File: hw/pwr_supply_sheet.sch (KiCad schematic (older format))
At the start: 14 parts

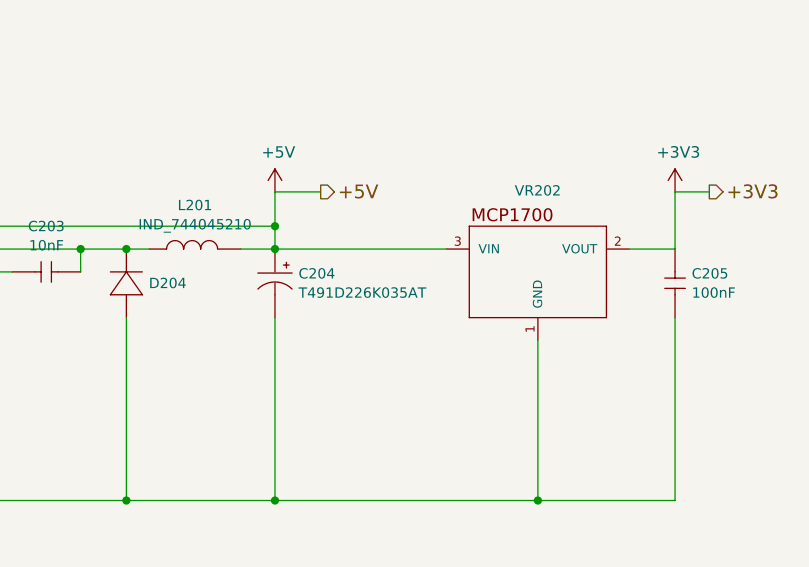
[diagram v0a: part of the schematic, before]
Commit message: 1.4.0 pcb created, tantalum caps changed to bigger ones
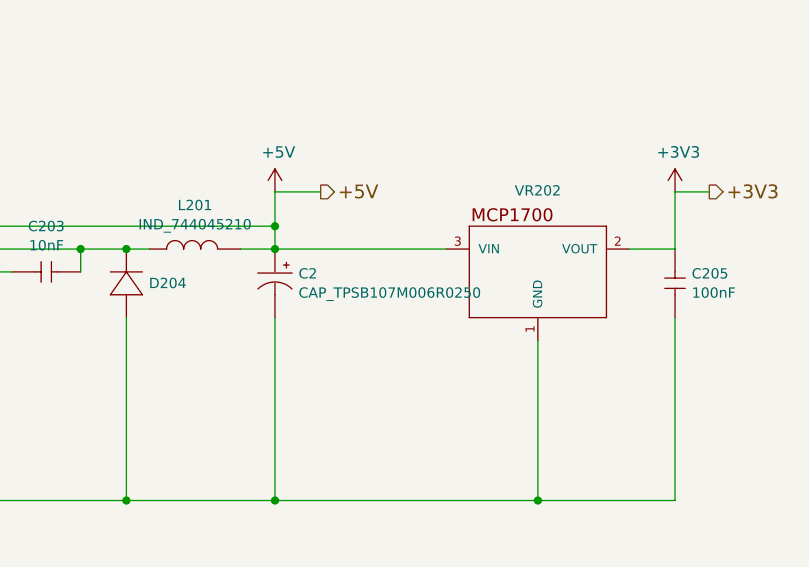
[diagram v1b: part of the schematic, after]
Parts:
- removed C204: T491D226K035AT, kemet:7343, symbol kemet:T491D226K035AT
- added C2: CAP_TPSB107M006R0250, usevolt:1210_CAP, symbol usevolt:CAP_TPSB107M006R0250
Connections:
- net +5V: now also C2.+
- net GND: now also C2.-
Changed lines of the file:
@@
-$EndComp
-$Comp
-L kemet:T491D226K035AT C204
-U 1 1 597AF606
-P 6850 4050
-F 0 "C204" V 6758 4153 45  0000 L CNN
-F 1 "T491D226K035AT" V 6842 4153 45  0000 L CNN
-F 2 "kemet:7343" H 6880 4200 20  0001 C CNN
-F 3 "http://www.farnell.com/datasheets/2121523.pdf?_ga=1.259966538.1948984246.1460023966" H 6850 3990 60  0001 C CNN
-F 4 "399-8375-1-ND" H 7450 4590 60  0001 C CNN "2nd Source Part Number"
-F 5 "Farnell" H 7150 4290 60  0001 C CNN "1st Source"
-F 6 "T491D226K035AT" H 7050 4190 60  0001 C CNN "Manufacturer Part Number"
-F 7 "Digikey" H 7350 4490 60  0001 C CNN "2nd Source"
-F 8 "Kemet" H 6950 4090 60  0001 C CNN "Manufacturer"
-F 9 "1457504" H 7250 4390 60  0001 C CNN "1st Source Part Number"
-	1    6850 4050
-	0    1    1    0
 $EndComp
 $Comp
@@
 	2550 2700 2900 2700
 Connection ~ 2900 2700
+$Comp
+L usevolt:CAP_TPSB107M006R0250 C2
+U 1 1 5C620853
+P 6850 4050
+F 0 "C2" V 6758 4153 45  0000 L CNN
+F 1 "CAP_TPSB107M006R0250" V 6842 4153 45  0000 L CNN
+F 2 "usevolt:1210_CAP" H 6880 4200 20  0001 C CNN
+F 3 "http://datasheets.avx.com/TPS.pdf" H 6850 3990 60  0001 C CNN
+F 4 "AVX Corporation" H 6950 4090 60  0001 C CNN "Manufacturer"
+F 5 "TPSB107M006R0250" H 7050 4190 60  0001 C CNN "Manufacturer Part Number"
+F 6 "Digi-Key" H 7150 4290 60  0001 C CNN "1st Source"
+F 7 "478-4978-1-ND" H 7250 4390 60  0001 C CNN "1st Source Part Number"
+F 8 "Mouser" H 7350 4490 60  0001 C CNN "2nd Source"
+F 9 "581-TPSB107M006R0250" H 7450 4590 60  0001 C CNN "2nd Source Part Number"
+	1    6850 4050
+	0    1    1    0
+$EndComp
 $EndSCHEMATC

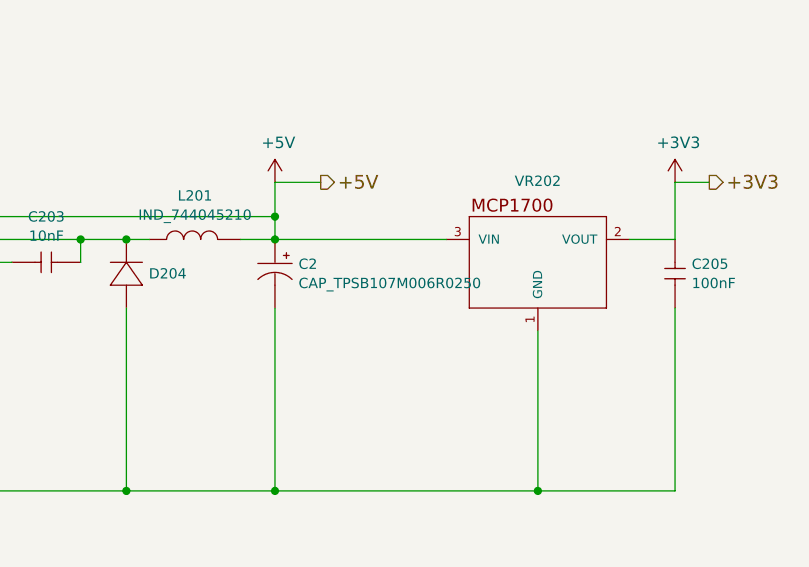
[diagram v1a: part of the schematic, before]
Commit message: hw 1.5.0, 2 ain inputs added
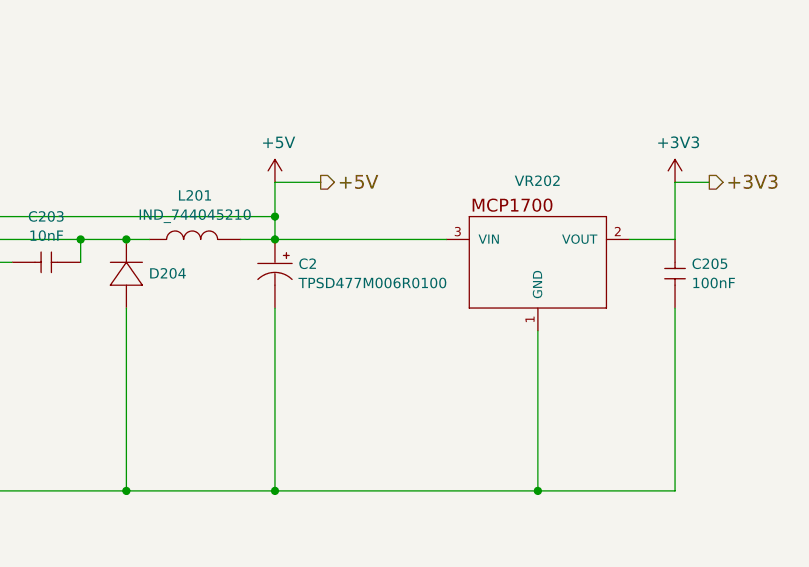
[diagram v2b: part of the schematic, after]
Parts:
- removed C2: CAP_TPSB107M006R0250, usevolt:1210_CAP, symbol usevolt:CAP_TPSB107M006R0250
- added C2: TPSD477M006R0100, usevolt:7343, symbol usevolt:TPSD477M006R0100
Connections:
- net +5V: now also C2.+
- net GND: now also C2.-
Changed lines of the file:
@@
 $Descr A4 11693 8268
 encoding utf-8
-Sheet 2 13
+Sheet 2 14
 Title "Power supply"
 Date "2016-08-20"
@@
 Connection ~ 2900 2700
 $Comp
-L usevolt:CAP_TPSB107M006R0250 C2
-U 1 1 5C620853
+L usevolt:TPSD477M006R0100 C2
+U 1 1 5D04E64E
 P 6850 4050
 F 0 "C2" V 6758 4153 45  0000 L CNN
-F 1 "CAP_TPSB107M006R0250" V 6842 4153 45  0000 L CNN
-F 2 "usevolt:1210_CAP" H 6880 4200 20  0001 C CNN
+F 1 "TPSD477M006R0100" V 6842 4153 45  0000 L CNN
+F 2 "usevolt:7343" H 6880 4200 20  0001 C CNN
 F 3 "http://datasheets.avx.com/TPS.pdf" H 6850 3990 60  0001 C CNN
-F 4 "AVX Corporation" H 6950 4090 60  0001 C CNN "Manufacturer"
-F 5 "TPSB107M006R0250" H 7050 4190 60  0001 C CNN "Manufacturer Part Number"
-F 6 "Digi-Key" H 7150 4290 60  0001 C CNN "1st Source"
-F 7 "478-4978-1-ND" H 7250 4390 60  0001 C CNN "1st Source Part Number"
-F 8 "Mouser" H 7350 4490 60  0001 C CNN "2nd Source"
-F 9 "581-TPSB107M006R0250" H 7450 4590 60  0001 C CNN "2nd Source Part Number"
+F 4 "478-1790-1-ND" H 7450 4590 60  0001 C CNN "2nd Source Part Number"
+F 5 "Farnell" H 7150 4290 60  0001 C CNN "1st Source"
+F 6 "TPSD477M006R0100" H 7050 4190 60  0001 C CNN "Manufacturer Part Number"
+F 7 "Digikey" H 7350 4490 60  0001 C CNN "2nd Source"
+F 8 "AVX Corporation" H 6950 4090 60  0001 C CNN "Manufacturer"
+F 9 "2852793" H 7250 4390 60  0001 C CNN "1st Source Part Number"
 	1    6850 4050
 	0    1    1    0
